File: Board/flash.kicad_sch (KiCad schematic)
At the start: 4 parts

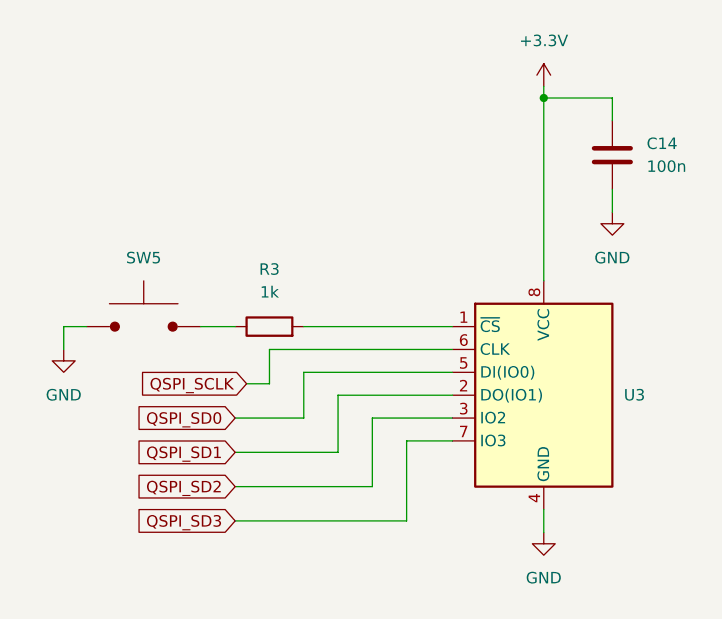
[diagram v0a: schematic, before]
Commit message: Touch-up module schematics
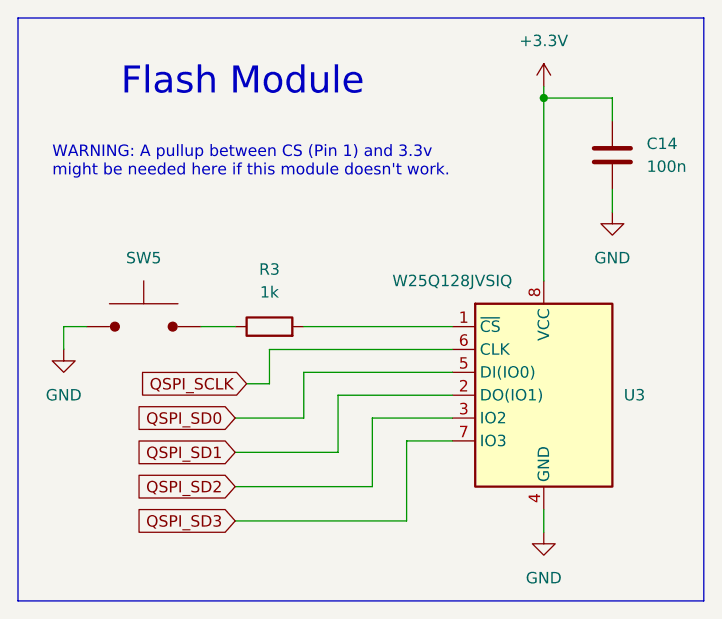
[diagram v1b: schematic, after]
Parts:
- U3: Name (none) -> W25Q128JVSIQ
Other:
- note added: "Flash Module"
- note added: "WARNING: A pullup between CS (Pin 1) and 3.3v might be needed here if this module doesn't work."
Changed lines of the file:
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@@
     (stroke (width 0) (type default))
+  )
+  (rectangle (start 101.6 31.75) (end 177.8 96.52)
+    (stroke (width 0) (type default))
+    (fill (type none))
+  )
+  (text "Flash Module" (at 113.03 40.64 0)
+    (effects (font (size 3 3)) (justify left bottom))
+  )
+  (text "WARNING: A pullup between CS (Pin 1) and 3.3v \nmight be needed here if this module doesn't work."
+    (at 105.41 49.53 0)
+    (effects (font (size 1.27 1.27)) (justify left bottom))
   )
   (global_label "QSPI_SCLK" (shape input) (at 127 72.39 180) (fields_autoplaced)
@@
   )
   (symbol (lib_id "ND68:W25Q128JVSIQ") (at 160.02 72.39 0) (unit 1)
-    (in_bom yes) (on_board yes) (dnp no) (fields_autoplaced)
+    (in_bom yes) (on_board yes) (dnp no)
     (property "Reference" "U3" (at 168.91 73.66 0)
       (effects (font (size 1.27 1.27)) (justify left))
@@
       (effects (font (size 1.27 1.27)) hide)
     )
+    (property "Name" "W25Q128JVSIQ" (at 149.86 60.96 0)
+      (effects (font (size 1.27 1.27)))
+    )
     (pin "7")

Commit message: Added the rest of the required stuff tp the mcu
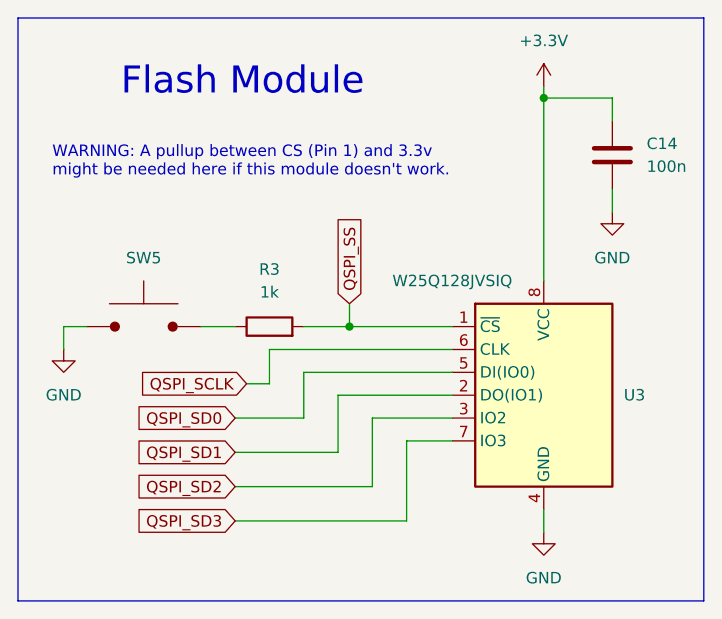
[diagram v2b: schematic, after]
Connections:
- net QSPI_SS: now reaches R3.2, U3.1 (~{CS})
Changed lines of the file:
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@@
   (junction (at 160.02 40.64) (diameter 0) (color 0 0 0 0)
+  )
+  (junction (at 138.43 66.04) (diameter 0) (color 0 0 0 0)
   )
   (wire (pts (xy 144.78 78.74) (xy 149.86 78.74))
@@
   )
   (wire (pts (xy 133.35 71.12) (xy 149.86 71.12))
+    (stroke (width 0) (type default))
+  )
+  (wire (pts (xy 138.43 63.5) (xy 138.43 66.04))
     (stroke (width 0) (type default))
   )
@@
     (stroke (width 0) (type default))
   )
-  (wire (pts (xy 133.35 66.04) (xy 149.86 66.04))
+  (wire (pts (xy 133.35 66.04) (xy 138.43 66.04))
     (stroke (width 0) (type default))
   )
@@
   )
   (wire (pts (xy 109.22 66.04) (xy 106.68 66.04))
+    (stroke (width 0) (type default))
+  )
+  (wire (pts (xy 138.43 66.04) (xy 149.86 66.04))
     (stroke (width 0) (type default))
   )
@@
     )
   )
+  (global_label "QSPI_SS" (shape input) (at 138.43 63.5 90) (fields_autoplaced)
+    (effects (font (size 1.27 1.27)) (justify left))
+    (property "Intersheetrefs" "${INTERSHEET_REFS}" (at 138.43 52.7134 90)
+      (effects (font (size 1.27 1.27)) (justify left) hide)
+    )
+  )

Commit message: Route mcu
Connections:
- net GND: now also SW5.1; no longer SW5.
- net at R3.1: now also SW5.2; no longer SW5.
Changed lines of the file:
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@@
       (effects (font (size 1.27 1.27)) hide)
     )
-    (pin "")
-    (pin "")
+    (pin "2")
+    (pin "1")
     (instances
       (project "ND68"

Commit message: Starting from scratch
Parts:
- renumbered SW5 to SW0
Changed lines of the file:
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@@
   (symbol (lib_id "ND68:PTS636_SM43_SMTR_LFS") (at 115.57 66.04 0) (unit 1)
     (in_bom yes) (on_board yes) (dnp no) (fields_autoplaced)
-    (property "Reference" "SW5" (at 115.57 58.42 0)
+    (property "Reference" "SW0" (at 115.57 58.42 0)
       (effects (font (size 1.27 1.27)))
     )
@@
       (project "ND68"
         (path "/f6515d16-f8c0-46c5-adb6-b60d73ae282b/38b3721d-c91c-4170-9bf9-33a48c8a26a3"
-          (reference "SW5") (unit 1)
+          (reference "SW0") (unit 1)
         )
       )

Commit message: Backing up"
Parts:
- added J4: Conn_01x02_Pin, Connector_PinHeader_2.54mm:PinHeader_1x02_P2.54mm_Vertical, symbol Connector:Conn_01x02_Pin
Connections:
- net GND: now also J4.2 (Pin_2)
- net at R3.1, SW0.2: now also J4.1 (Pin_1)
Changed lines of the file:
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@@
   (junction (at 160.02 40.64) (diameter 0) (color 0 0 0 0)
   )
+  (junction (at 107.95 66.04) (diameter 0) (color 0 0 0 0)
+  )
+  (junction (at 123.19 66.04) (diameter 0) (color 0 0 0 0)
+  )
   (junction (at 138.43 66.04) (diameter 0) (color 0 0 0 0)
+  )
+  (wire (pts (xy 107.95 55.88) (xy 107.95 66.04))
+    (stroke (width 0) (type default))
   )
   (wire (pts (xy 144.78 78.74) (xy 149.86 78.74))
@@
   )
   (wire (pts (xy 160.02 40.64) (xy 167.64 40.64))
+    (stroke (width 0) (type default))
+  )
+  (wire (pts (xy 114.3 55.88) (xy 107.95 55.88))
     (stroke (width 0) (type default))
   )
@@
     (stroke (width 0) (type default))
   )
+  (wire (pts (xy 123.19 55.88) (xy 123.19 66.04))
+    (stroke (width 0) (type default))
+  )
   (wire (pts (xy 167.64 40.64) (xy 167.64 43.18))
     (stroke (width 0) (type default))
@@
     (stroke (width 0) (type default))
   )
+  (wire (pts (xy 107.95 66.04) (xy 106.68 66.04))
+    (stroke (width 0) (type default))
+  )
   (wire (pts (xy 129.54 68.58) (xy 149.86 68.58))
     (stroke (width 0) (type default))
   )
-  (wire (pts (xy 121.92 66.04) (xy 125.73 66.04))
+  (wire (pts (xy 121.92 66.04) (xy 123.19 66.04))
     (stroke (width 0) (type default))
   )
@@
     (stroke (width 0) (type default))
   )
+  (wire (pts (xy 116.84 55.88) (xy 123.19 55.88))
+    (stroke (width 0) (type default))
+  )
   (wire (pts (xy 137.16 73.66) (xy 149.86 73.66))
     (stroke (width 0) (type default))
   )
-  (wire (pts (xy 109.22 66.04) (xy 106.68 66.04))
+  (wire (pts (xy 109.22 66.04) (xy 107.95 66.04))
     (stroke (width 0) (type default))
   )
@@
   )
   (wire (pts (xy 160.02 39.37) (xy 160.02 40.64))
+    (stroke (width 0) (type default))
+  )
+  (wire (pts (xy 123.19 66.04) (xy 125.73 66.04))
     (stroke (width 0) (type default))
   )
@@
     )
   )
+  (symbol (lib_id "Connector:Conn_01x02_Pin") (at 116.84 50.8 270) (unit 1)
+    (in_bom yes) (on_board yes) (dnp no)
+    (property "Reference" "J4" (at 118.11 52.07 90)
+      (effects (font (size 1.27 1.27)) (justify left))
+    )
+    (property "Value" "Conn_01x02_Pin" (at 118.11 52.705 90)
+      (effects (font (size 1.27 1.27)) (justify left) hide)
+    )
+    (property "Footprint" "Connector_PinHeader_2.54mm:PinHeader_1x02_P2.54mm_Vertical" (at 116.84 50.8 0)
+      (effects (font (size 1.27 1.27)) hide)
+    )
+    (property "Datasheet" "~" (at 116.84 50.8 0)
+      (effects (font (size 1.27 1.27)) hide)
+    )
+    (pin "1")
+    (pin "2")
+    (instances
+      (project "ND68"
+        (path "/f6515d16-f8c0-46c5-adb6-b60d73ae282b/38b3721d-c91c-4170-9bf9-33a48c8a26a3"
+          (reference "J4") (unit 1)
+        )
+      )
+    )
+  )
